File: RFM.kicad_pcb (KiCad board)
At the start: 2 copper layers, 27 parts, among them P1 USB_OTG, Y1 40MHz, Y2 8MHz(16pF)

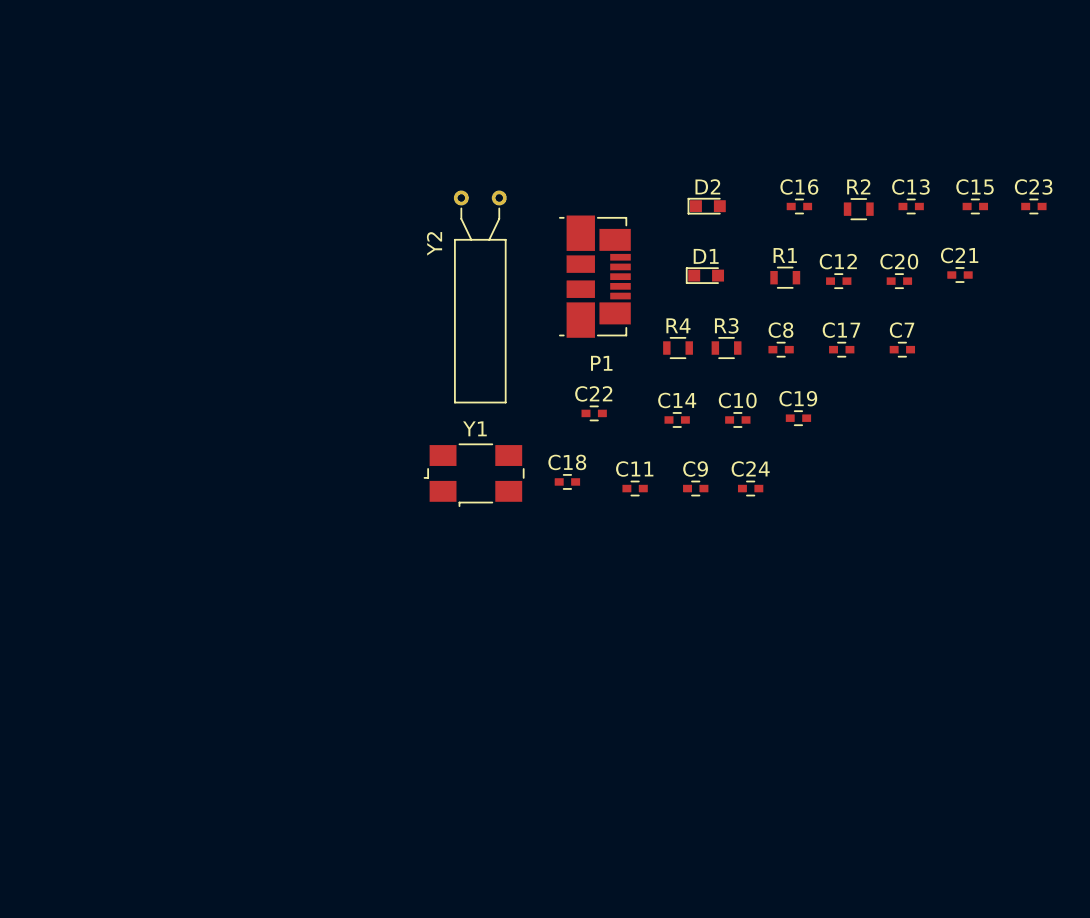
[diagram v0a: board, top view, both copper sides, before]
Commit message: Balun footprint
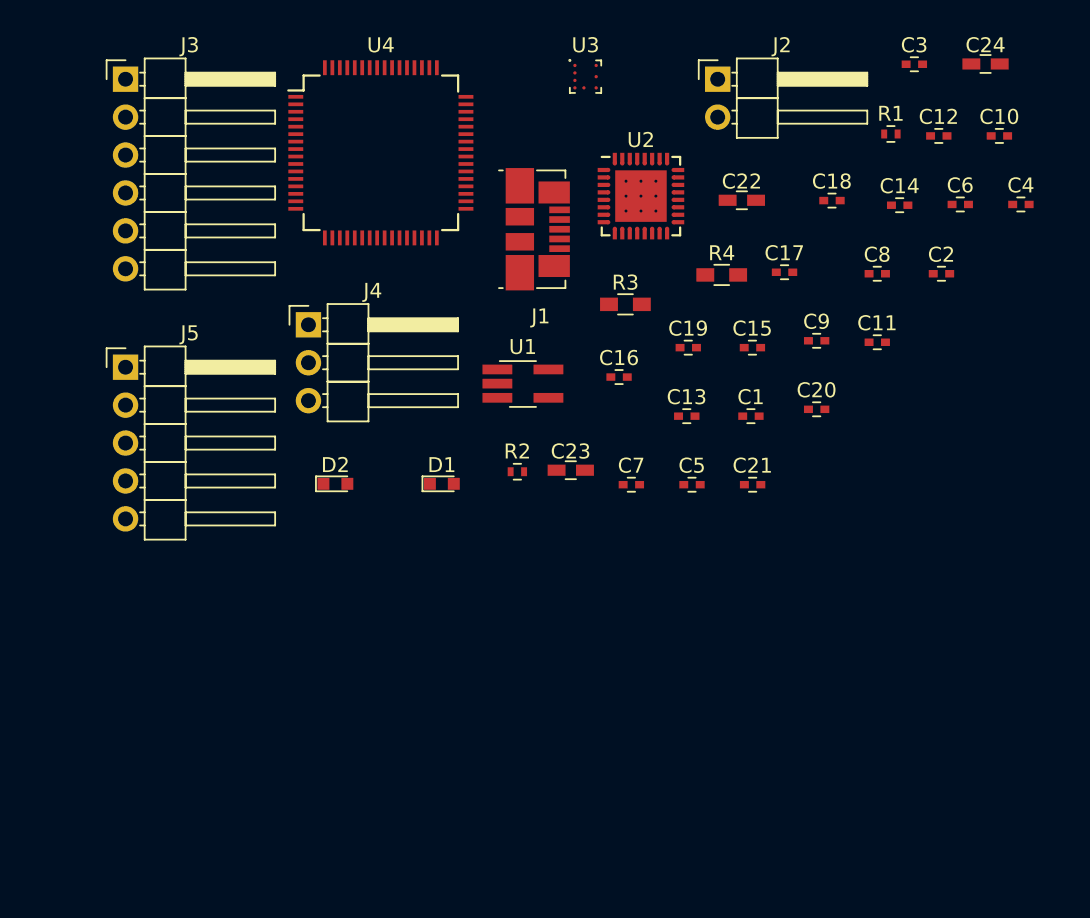
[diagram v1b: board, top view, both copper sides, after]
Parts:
- removed P1: USB_OTG, Connectors_Molex:USB_Micro-B_Molex_47346-0001
- removed Y1: 40MHz, Crystals:Crystal_SMD_0603-4pin_6.0x3.5mm
- removed Y2: 8MHz(16pF), Crystals:Crystal_AT310_d3.0mm_l10.0mm_Horizontal
- added C1: 0.1uF, Capacitors_SMD:C_0402, F.Cu at (179.6, 114.7)
- added C2: 2.2uF, Capacitors_SMD:C_0402, F.Cu at (192.4, 105.2)
- added C3: 0.01uF, Capacitors_SMD:C_0402, F.Cu at (190.5, 91.1)
- added C4: 47nF, Capacitors_SMD:C_0402, F.Cu at (197.7, 100.5)
- added C5: 47nF, Capacitors_SMD:C_0402, F.Cu at (175.7, 119.3)
- added C6: 47nF, Capacitors_SMD:C_0402, F.Cu at (193.6, 100.5)
- added J1: USB_OTG, Connectors_Molex:USB_Micro-B_Molex_47346-0001, F.Cu at (165.5, 102.2)
- added J2: CONN_PWR, Pin_Headers:Pin_Header_Angled_1x02_Pitch2.54mm, F.Cu at (177.4, 92.1)
- added J3: CONN_DEBUG, Pin_Headers:Pin_Header_Angled_1x06_Pitch2.54mm, F.Cu at (137.7, 92.1)
- added J4: CONN_USART, Pin_Headers:Pin_Header_Angled_1x03_Pitch2.54mm, F.Cu at (150.0, 108.6)
- added J5: CONN_SPI, Pin_Headers:Pin_Header_Angled_1x05_Pitch2.54mm, F.Cu at (137.7, 111.4)
- added U1: TPS79333, TO_SOT_Packages_SMD:TSOT-23-5_HandSoldering, F.Cu at (164.3, 112.5)
- added U2: CC1200, CC1200:CC1200, F.Cu at (172.2, 100.0)
- added U3: BALF-112X-02D3, CC1200:BALF-112X-02D3, F.Cu at (168.5, 92.0)
- added U4: STM32F103R8Tx, Housings_QFP:LQFP-64_10x10mm_Pitch0.5mm, F.Cu at (154.8, 97.1)
- C22, C23, C24: footprint Capacitors_SMD:C_0402 -> Capacitors_SMD:C_0603_HandSoldering
- R1: value 56k -> 18; footprint Resistors_SMD:R_0603 -> Resistors_SMD:R_0402
- R2: value 18 -> 56k; footprint Resistors_SMD:R_0603 -> Resistors_SMD:R_0402
- R3, R4: footprint Resistors_SMD:R_0603 -> Resistors_SMD:R_0603_HandSoldering
- moved C23 35.7 mm to (167.5, 118.3)
- moved C24 32.5 mm to (195.3, 91.1)
- moved D2 31.1 mm to (151.8, 119.2)
- moved R2 28.8 mm to (164.0, 118.4)
- moved C18 25.9 mm to (185.0, 100.3)
- moved C10 25.9 mm to (196.2, 95.9)
- moved D1 22.5 mm to (158.9, 119.2)
- moved C14 20.7 mm to (189.6, 100.6)
- moved C13 20.6 mm to (175.3, 114.7)
- moved C7 20.3 mm to (171.6, 119.3)
- moved C21 19.8 mm to (179.7, 119.3)
- moved C11 18.9 mm to (188.1, 109.8)
- moved C15 17.7 mm to (179.7, 110.1)
- moved C22 17.4 mm to (179.0, 100.3)
- moved C16 16.6 mm to (170.8, 112.1)
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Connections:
- R1 pad 1: Net-(R1-Pad1) -> Net-(C17-Pad1)
- R1 pad 2: GND -> VDD
- R2 pad 1: Net-(C17-Pad1) -> Net-(R2-Pad1)
- R2 pad 2: VDD -> GND

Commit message: Update footprints
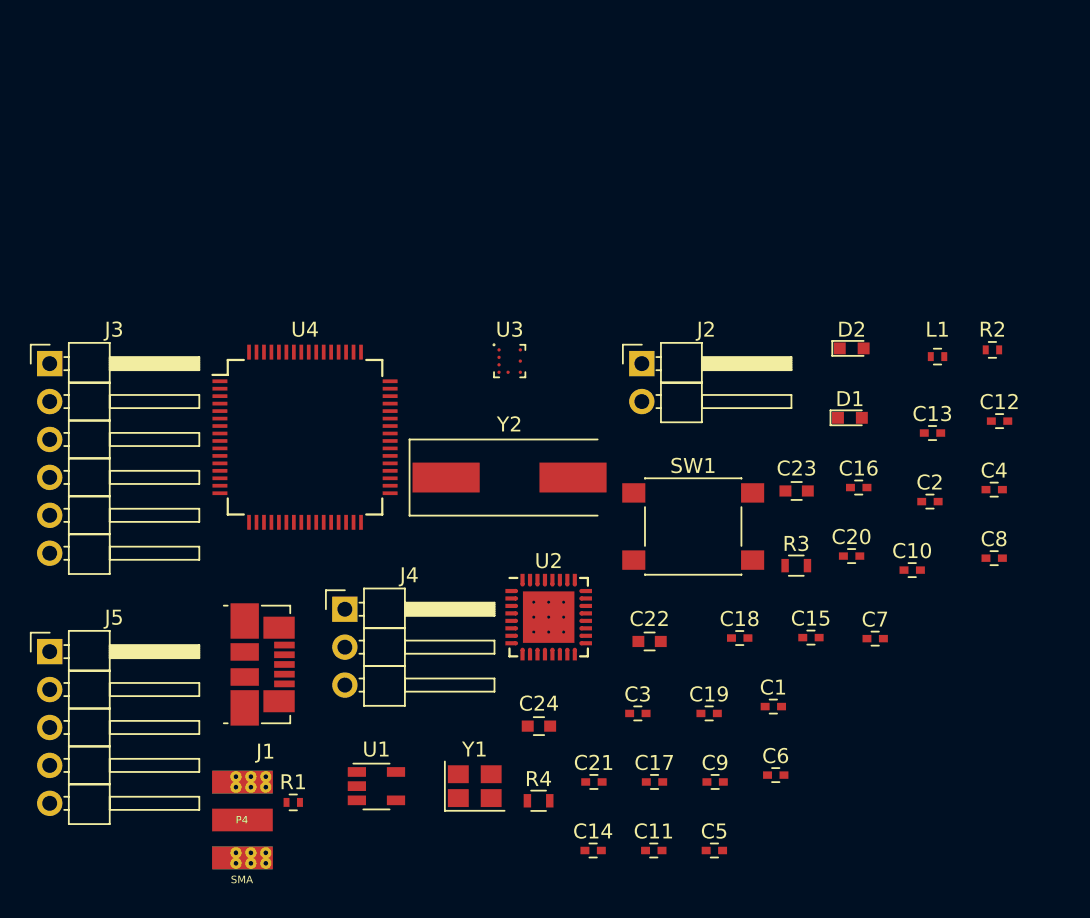
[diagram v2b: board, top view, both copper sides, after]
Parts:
- added L1: 56nH, Inductors_SMD:L_0402, F.Cu at (192.1, 110.7)
- added P4: SMA, gsg-modules:SMA-EDGE, F.Cu at (143.5, 141.8)
- added SW1: SW_Push, Buttons_Switches_SMD:SW_SPST_PTS645, F.Cu at (175.7, 122.1)
- added Y1: 40MHz, CC1200:NX3225SA-40M-EXS00A-CS03880, F.Cu at (161.1, 139.5)
- added Y2: 8MHz(16pF), Crystals:Crystal_SMD_HC49-SD, F.Cu at (163.4, 118.8)
- C22, C23, C24: footprint Capacitors_SMD:C_0603_HandSoldering -> Capacitors_SMD:C_0603
- R3, R4: footprint Resistors_SMD:R_0603_HandSoldering -> Resistors_SMD:R_0603
- U1: footprint TO_SOT_Packages_SMD:TSOT-23-5_HandSoldering -> TO_SOT_Packages_SMD:TSOT-23-5
- moved R1 60.1 mm to (148.9, 140.6)
- moved C24 53.5 mm to (165.4, 135.5)
- moved C14 47.8 mm to (169.0, 143.8)
- moved C3 47.3 mm to (172.0, 134.6)
- moved C6 40.2 mm to (181.3, 138.8)
- moved R4 37.3 mm to (165.4, 140.5)
- moved C11 37.2 mm to (173.1, 143.8)
- moved D2 35.7 mm to (186.3, 110.2)
- moved C17 35.2 mm to (173.1, 139.2)
- moved J1 34.5 mm to (147.0, 131.3)
- moved R2 32.8 mm to (195.8, 110.3)
- moved C9 30.3 mm to (177.2, 139.2)
- moved C22 30.2 mm to (172.8, 129.8)
- moved C18 29.9 mm to (178.8, 129.6)
- moved C10 29.7 mm to (190.4, 125.0)
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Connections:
- U3 pad C1: (no net) -> Net-(P4-Pad1)
